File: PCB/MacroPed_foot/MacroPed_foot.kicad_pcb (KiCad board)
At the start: 2 copper layers, 22.9 x 52.1 mm, 6 parts, among them J9 Conn_01x02_Socket, SW1 SW_SPST

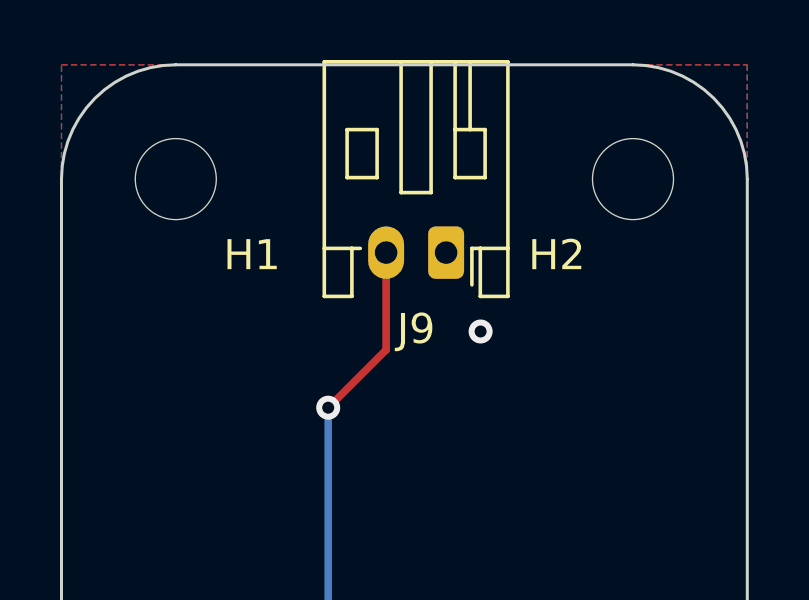
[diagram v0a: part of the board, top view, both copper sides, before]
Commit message: Move jst to back of pedal to save on SMT
Signed-off-by: Devnol <pgkoutsoumanis@gmail.com>
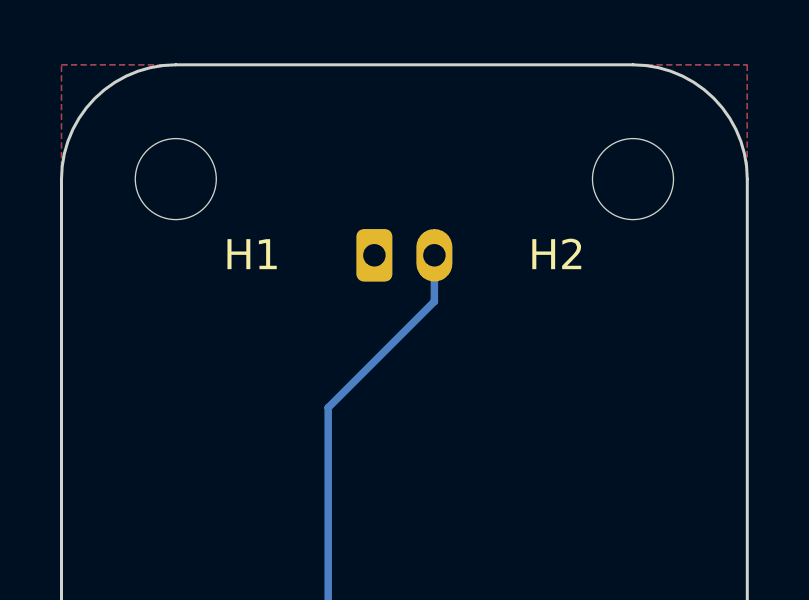
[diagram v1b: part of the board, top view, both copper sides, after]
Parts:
- J9: moved to B.Cu
- moved J9 2.39 mm to (104.4, 27.9), turned to 0 degrees
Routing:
- net Net-(J9-Pin_2): track 16.7 -> 17.3 mm, vias 1 -> 0
- net /Foot_GND: vias 2 -> 1

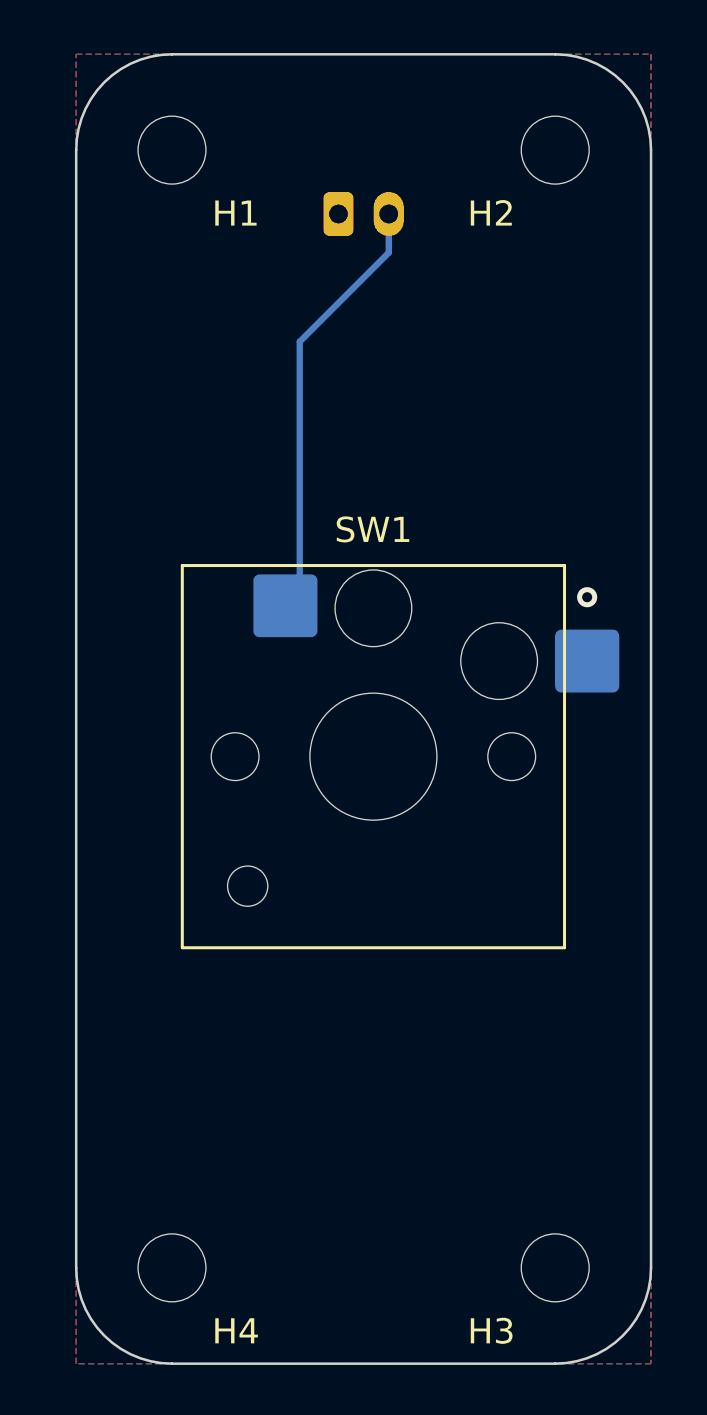
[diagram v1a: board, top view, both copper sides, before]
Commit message: Change board dimensions to real units
Signed-off-by: Devnol <pgkoutsoumanis@gmail.com>
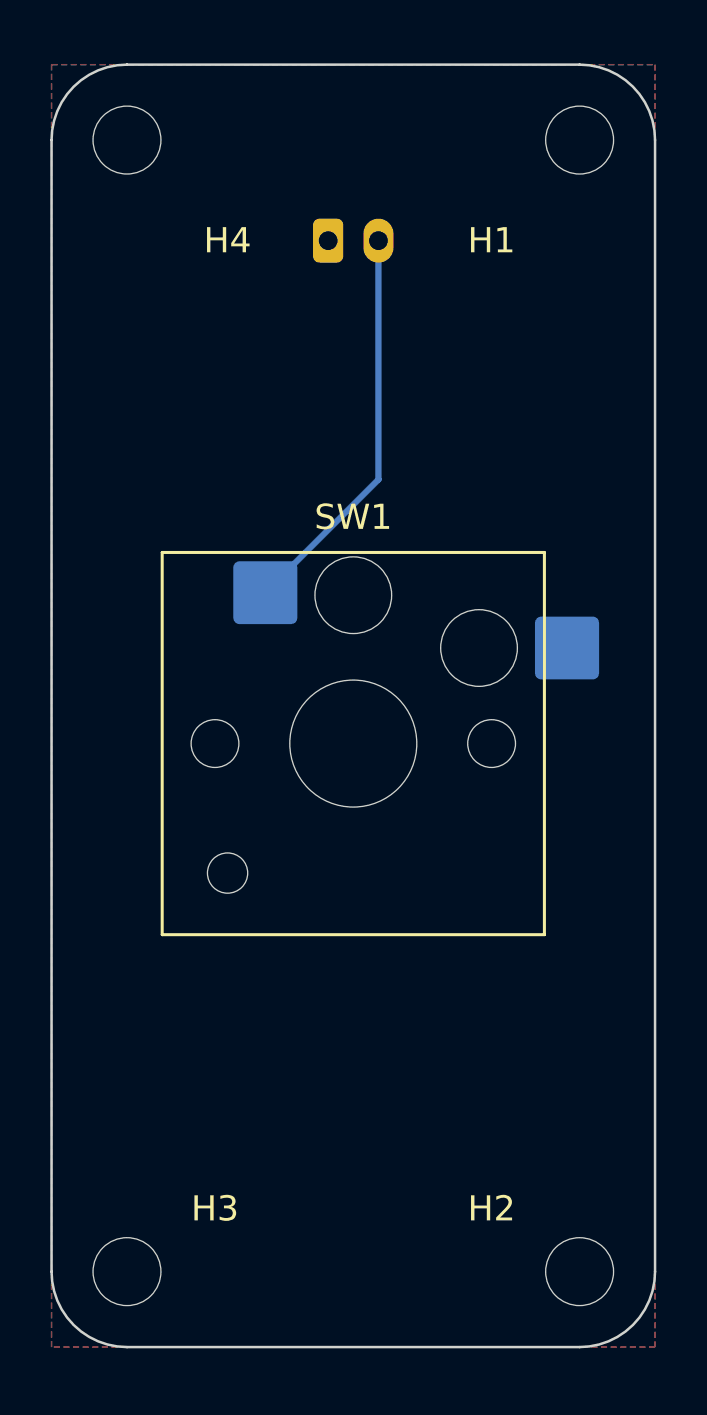
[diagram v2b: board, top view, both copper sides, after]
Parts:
- moved H4 44.9 mm to (96.0, 25.0)
- moved H2 44.6 mm to (114.0, 70.0)
- moved H3 17.0 mm to (96.0, 70.0)
- moved H1 16.2 mm to (114.0, 25.0)
- moved J9 1.14 mm to (104.0, 29.0)
- moved SW1 0.95 mm to (105.0, 49.0)
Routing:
- net Net-(J9-Pin_2): track 17.3 -> 15.9 mm
- net /Foot_GND: vias 1 -> 0
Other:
- board size 22.9 x 52.1 mm -> 24 x 51 mm
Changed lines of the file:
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@@
   (net 2 "/Foot_GND")
   (footprint "PCM_Switch_Keyboard_Hotswap_Kailh:SW_Hotswap_Kailh_Choc_V1V2_2.00u_90deg" (layer "F.Cu")
-    (at 105.8 49.52)
+    (at 105 49)
     (descr "Kailh Choc keyswitch V1V2 CPG1350 V1 CPG1353 V2 Hotswap Keycap 2.00u 90deg")
     (tags "Kailh Choc Keyswitch Switch CPG1350 V1 CPG1353 V2 Hotswap Cutout Keycap 2.00u 90deg")
@@
   )
   (footprint "MountingHole:MountingHole_2.7mm_M2.5_DIN965" (layer "F.Cu")
-    (at 97.79 69.85)
+    (at 96 25)
     (descr "Mounting Hole 2.7mm, no annular, M2.5, DIN965")
     (tags "mounting hole 2.7mm no annular m2.5 din965")
@@
     (property "ki_keywords" "mounting hole")
     (attr exclude_from_pos_files)
-    (fp_text reference "H4" (at 2.54 2.54) (layer "F.SilkS")
+    (fp_text reference "H4" (at 4 4) (layer "F.SilkS")
         (effects (font (size 1 1) (thickness 0.15)))
     )
@@
   )
   (footprint "MountingHole:MountingHole_2.7mm_M2.5_DIN965" (layer "F.Cu")
-    (at 97.79 25.4)
+    (at 114 25)
     (descr "Mounting Hole 2.7mm, no annular, M2.5, DIN965")
     (tags "mounting hole 2.7mm no annular m2.5 din965")
@@
     (property "ki_keywords" "mounting hole")
     (attr exclude_from_pos_files)
-    (fp_text reference "H1" (at 2.54 2.54) (layer "F.SilkS")
+    (fp_text reference "H1" (at -3.5 4) (layer "F.SilkS")
         (effects (font (size 1 1) (thickness 0.15)))
     )
@@
   )
   (footprint "MountingHole:MountingHole_2.7mm_M2.5_DIN965" (layer "F.Cu")
-    (at 113.03 25.4)
+    (at 114 70)
     (descr "Mounting Hole 2.7mm, no annular, M2.5, DIN965")
     (tags "mounting hole 2.7mm no annular m2.5 din965")
@@
     (property "ki_keywords" "mounting hole")
     (attr exclude_from_pos_files)
-    (fp_text reference "H2" (at -2.54 2.54) (layer "F.SilkS")
+    (fp_text reference "H2" (at -3.5 -2.5) (layer "F.SilkS")
         (effects (font (size 1 1) (thickness 0.15)))
     )
@@
   )
   (footprint "MountingHole:MountingHole_2.7mm_M2.5_DIN965" (layer "F.Cu")
-    (at 113.03 69.85)
+    (at 96 70)
     (descr "Mounting Hole 2.7mm, no annular, M2.5, DIN965")
     (tags "mounting hole 2.7mm no annular m2.5 din965")
@@
     (property "ki_keywords" "mounting hole")
     (attr exclude_from_pos_files)
-    (fp_text reference "H3" (at -2.54 2.54) (layer "F.SilkS")
+    (fp_text reference "H3" (at 3.5 -2.5) (layer "F.SilkS")
         (effects (font (size 1 1) (thickness 0.15)))
     )
@@
   )
   (footprint "Connector_JST:JST_PH_S2B-PH-K_1x02_P2.00mm_Horizontal" (layer "B.Cu")
-    (at 104.41 27.94)
+    (at 104 29)
     (descr "JST PH series connector, S2B-PH-K (http://www.jst-mfg.com/product/pdf/eng/ePH.pdf), generated with kicad-footprint-generator")
     (tags "connector JST PH top entry")
@@
     )
   )
-  (gr_line (start 113.03 73.66) (end 97.79 73.66)
-    (stroke (width 0.1) (type default)) (layer "Edge.Cuts"))
-  (gr_line (start 116.84 25.4) (end 116.84 69.85)
-    (stroke (width 0.1) (type default)) (layer "Edge.Cuts"))
-  (gr_line (start 97.79 21.59) (end 113.03 21.59)
-    (stroke (width 0.1) (type default)) (layer "Edge.Cuts"))
-  (gr_arc (start 97.79 73.66) (mid 95.095923 72.544077) (end 93.98 69.85)
-    (stroke (width 0.1) (type default)) (layer "Edge.Cuts"))
-  (gr_line (start 93.98 69.85) (end 93.98 25.4)
-    (stroke (width 0.1) (type default)) (layer "Edge.Cuts"))
-  (gr_arc (start 116.84 69.85) (mid 115.724077 72.544077) (end 113.03 73.66)
-    (stroke (width 0.1) (type default)) (layer "Edge.Cuts"))
-  (gr_arc (start 113.03 21.59) (mid 115.724077 22.705923) (end 116.84 25.4)
-    (stroke (width 0.1) (type default)) (layer "Edge.Cuts"))
-  (gr_arc (start 93.98 25.4) (mid 95.095923 22.705923) (end 97.79 21.59)
-    (stroke (width 0.1) (type default)) (layer "Edge.Cuts"))
-  (segment (start 106.41 27.94) (end 106.41 29.48) (width 0.25) (layer "B.Cu") (net 1))
-  (segment (start 106.41 29.48) (end 102.87 33.02) (width 0.25) (layer "B.Cu") (net 1))
-  (segment (start 102.87 42.95) (end 102.87 33.02) (width 0.25) (layer "B.Cu") (net 1))
-  (segment (start 102.3 43.52) (end 102.87 42.95) (width 0.25) (layer "B.Cu") (net 1))
-  (via (at 114.3 43.18) (size 0.8) (drill 0.4) (layers "F.Cu" "B.Cu") (free) (net 2))
-  (zone (net 2) (net_name "/Foot_GND") (layer "F.Cu") (name "GND") (hatch edge 0.5)
-    (priority 1)
-    (connect_pads thru_hole_only (clearance 0.5))
+  (gr_arc (start 117 70) (mid 116.12132 72.12132) (end 114 73)
+    (stroke (width 0.1) (type default)) (layer "Edge.Cuts"))
+  (gr_line (start 96 22) (end 114 22)
+    (stroke (width 0.1) (type default)) (layer "Edge.Cuts"))
+  (gr_arc (start 114 22) (mid 116.12132 22.87868) (end 117 25)
+    (stroke (width 0.1) (type default)) (layer "Edge.Cuts"))
+  (gr_arc (start 96 73) (mid 93.87868 72.12132) (end 93 70)
+    (stroke (width 0.1) (type default)) (layer "Edge.Cuts"))
+  (gr_arc (start 93 25) (mid 93.87868 22.87868) (end 96 22)
+    (stroke (width 0.1) (type default)) (layer "Edge.Cuts"))
+  (gr_line (start 117 25) (end 117 70)
+    (stroke (width 0.1) (type default)) (layer "Edge.Cuts"))
+  (gr_line (start 93 70) (end 93 25)
+    (stroke (width 0.1) (type default)) (layer "Edge.Cuts"))
+  (gr_line (start 114 73) (end 96 73)
+    (stroke (width 0.1) (type default)) (layer "Edge.Cuts"))
+  (segment (start 106 29) (end 106 38.5) (width 0.25) (layer "B.Cu") (net 1))
+  (segment (start 106 38.5) (end 101.5 43) (width 0.25) (layer "B.Cu") (net 1))
+  (zone (net 2) (net_name "/Foot_GND") (layer "F.Cu") (hatch edge 0.5)
+    (connect_pads (clearance 0.5))
     (min_thickness 0.25) (filled_areas_thickness no)
-    (fill yes (thermal_gap 0.5) (thermal_bridge_width 0.5) (island_removal_mode 2) (island_area_min 2))
+    (fill yes (thermal_gap 0.5) (thermal_bridge_width 0.5))
     (polygon
       (pts
-        (xy 93.98 21.59)
-        (xy 116.84 21.59)
-        (xy 116.84 73.66)
-        (xy 93.98 73.66)
+        (xy 93 22)
+        (xy 117 22)
+        (xy 117 73)
+        (xy 93 73)
       )
     )
   )
-  (zone (net 2) (net_name "/Foot_GND") (layer "B.Cu") (name "GND") (hatch edge 0.5)
-    (priority 2)
-    (connect_pads thru_hole_only (clearance 0.5))
+  (zone (net 2) (net_name "/Foot_GND") (layer "B.Cu") (hatch edge 0.5)
+    (priority 1)
+    (connect_pads (clearance 0.5))
     (min_thickness 0.25) (filled_areas_thickness no)
-    (fill yes (thermal_gap 0.5) (thermal_bridge_width 0.5) (island_removal_mode 2) (island_area_min 2))
+    (fill yes (thermal_gap 0.5) (thermal_bridge_width 0.5))
     (polygon
       (pts
-        (xy 93.98 21.59)
-        (xy 116.84 21.59)
-        (xy 116.84 73.66)
-        (xy 93.98 73.66)
+        (xy 93 22)
+        (xy 117 22)
+        (xy 117 73)
+        (xy 93 73)
       )
     )
